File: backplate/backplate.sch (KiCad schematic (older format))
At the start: 1 part, among them J1 Conn_01x01_Male

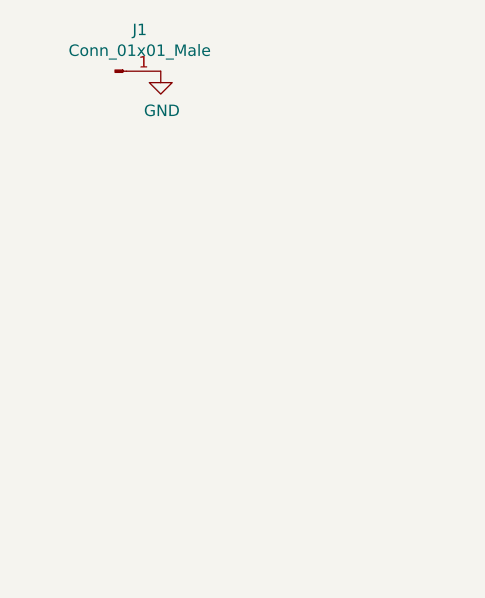
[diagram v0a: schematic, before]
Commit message: need to create models to check board compatibility; prototype candidate
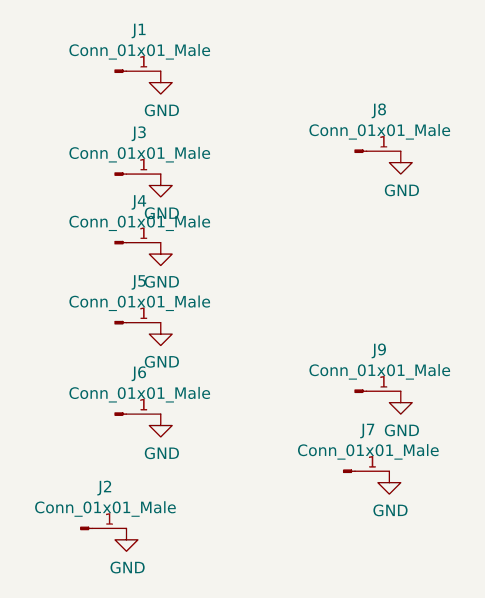
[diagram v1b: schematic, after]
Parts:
- added J2, J3, J4, J5, J6, J7, J8, J9: Conn_01x01_Male, backplate:sound_mounting_hole, symbol Connector:Conn_01x01_Male
- J1: footprint (none) -> backplate:sound_mounting_hole
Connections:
- net GND: now also J2.1 (Pin_1), J3.1 (Pin_1), J4.1 (Pin_1), J5.1 (Pin_1), J6.1 (Pin_1), J7.1 (Pin_1), J8.1 (Pin_1), J9.1 (Pin_1)
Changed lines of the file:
@@
 $EndDescr
-$Comp
-L Connector:Conn_01x01_Male J1
-U 1 1 5EB515EA
-P 3150 3350
-F 0 "J1" H 3258 3531 50  0000 C CNN
-F 1 "Conn_01x01_Male" H 3258 3440 50  0000 C CNN
-F 2 "" H 3150 3350 50  0001 C CNN
-F 3 "~" H 3150 3350 50  0001 C CNN
-	1    3150 3350
-	1    0    0    -1
-$EndComp
 $Comp
 L power:GND #PWR?
@@
 	1    0    0    -1
 $EndComp
+$Comp
+L Connector:Conn_01x01_Male J1
+U 1 1 5EB515EA
+P 3150 3350
+F 0 "J1" H 3258 3531 50  0000 C CNN
+F 1 "Conn_01x01_Male" H 3258 3440 50  0000 C CNN
+F 2 "backplate:sound_mounting_hole" H 3150 3350 50  0001 C CNN
+F 3 "~" H 3150 3350 50  0001 C CNN
+	1    3150 3350
+	1    0    0    -1
+$EndComp
+$Comp
+L power:GND #PWR?
+U 1 1 5EC17961
+P 3350 3800
+F 0 "#PWR?" H 3350 3550 50  0001 C CNN
+F 1 "GND" H 3355 3627 50  0000 C CNN
+F 2 "" H 3350 3800 50  0001 C CNN
+F 3 "" H 3350 3800 50  0001 C CNN
+	1    3350 3800
+	1    0    0    -1
+$EndComp
+$Comp
+L Connector:Conn_01x01_Male J3
+U 1 1 5EC17967
+P 3150 3800
+F 0 "J3" H 3258 3981 50  0000 C CNN
+F 1 "Conn_01x01_Male" H 3258 3890 50  0000 C CNN
+F 2 "backplate:sound_mounting_hole" H 3150 3800 50  0001 C CNN
+F 3 "~" H 3150 3800 50  0001 C CNN
+	1    3150 3800
+	1    0    0    -1
+$EndComp
+$Comp
+L power:GND #PWR?
+U 1 1 5EC17B1F
+P 3350 4100
+F 0 "#PWR?" H 3350 3850 50  0001 C CNN
+F 1 "GND" H 3355 3927 50  0000 C CNN
+F 2 "" H 3350 4100 50  0001 C CNN
+F 3 "" H 3350 4100 50  0001 C CNN
+	1    3350 4100
+	1    0    0    -1
+$EndComp
+$Comp
+L Connector:Conn_01x01_Male J4
+U 1 1 5EC17B25
+P 3150 4100
+F 0 "J4" H 3258 4281 50  0000 C CNN
+F 1 "Conn_01x01_Male" H 3258 4190 50  0000 C CNN
+F 2 "backplate:sound_mounting_hole" H 3150 4100 50  0001 C CNN
+F 3 "~" H 3150 4100 50  0001 C CNN
+	1    3150 4100
+	1    0    0    -1
+$EndComp
+$Comp
+L power:GND #PWR?
+U 1 1 5EC17CFB
+P 3350 4450
+F 0 "#PWR?" H 3350 4200 50  0001 C CNN
+F 1 "GND" H 3355 4277 50  0000 C CNN
+F 2 "" H 3350 4450 50  0001 C CNN
+F 3 "" H 3350 4450 50  0001 C CNN
+	1    3350 4450
+	1    0    0    -1
+$EndComp
+$Comp
+L Connector:Conn_01x01_Male J5
+U 1 1 5EC17D01
+P 3150 4450
+F 0 "J5" H 3258 4631 50  0000 C CNN
+F 1 "Conn_01x01_Male" H 3258 4540 50  0000 C CNN
+F 2 "backplate:sound_mounting_hole" H 3150 4450 50  0001 C CNN
+F 3 "~" H 3150 4450 50  0001 C CNN
+	1    3150 4450
+	1    0    0    -1
+$EndComp
+$Comp
+L power:GND #PWR?
+U 1 1 5EC1804B
+P 3350 4850
+F 0 "#PWR?" H 3350 4600 50  0001 C CNN
+F 1 "GND" H 3355 4677 50  0000 C CNN
+F 2 "" H 3350 4850 50  0001 C CNN
+F 3 "" H 3350 4850 50  0001 C CNN
+	1    3350 4850
+	1    0    0    -1
+$EndComp
+$Comp
+L Connector:Conn_01x01_Male J6
+U 1 1 5EC18051
+P 3150 4850
+F 0 "J6" H 3258 5031 50  0000 C CNN
+F 1 "Conn_01x01_Male" H 3258 4940 50  0000 C CNN
+F 2 "backplate:sound_mounting_hole" H 3150 4850 50  0001 C CNN
+F 3 "~" H 3150 4850 50  0001 C CNN
+	1    3150 4850
+	1    0    0    -1
+$EndComp
+$Comp
+L power:GND #PWR?
+U 1 1 5EC18207
+P 3200 5350
+F 0 "#PWR?" H 3200 5100 50  0001 C CNN
+F 1 "GND" H 3205 5177 50  0000 C CNN
+F 2 "" H 3200 5350 50  0001 C CNN
+F 3 "" H 3200 5350 50  0001 C CNN
+	1    3200 5350
+	1    0    0    -1
+$EndComp
+$Comp
+L Connector:Conn_01x01_Male J2
+U 1 1 5EC1820D
+P 3000 5350
+F 0 "J2" H 3108 5531 50  0000 C CNN
+F 1 "Conn_01x01_Male" H 3108 5440 50  0000 C CNN
+F 2 "backplate:sound_mounting_hole" H 3000 5350 50  0001 C CNN
+F 3 "~" H 3000 5350 50  0001 C CNN
+	1    3000 5350
+	1    0    0    -1
+$EndComp
+$Comp
+L power:GND #PWR?
+U 1 1 5EC182CD
+P 4400 4750
+F 0 "#PWR?" H 4400 4500 50  0001 C CNN
+F 1 "GND" H 4405 4577 50  0000 C CNN
+F 2 "" H 4400 4750 50  0001 C CNN
+F 3 "" H 4400 4750 50  0001 C CNN
+	1    4400 4750
+	1    0    0    -1
+$EndComp
+$Comp
+L Connector:Conn_01x01_Male J9
+U 1 1 5EC182D3
+P 4200 4750
+F 0 "J9" H 4308 4931 50  0000 C CNN
+F 1 "Conn_01x01_Male" H 4308 4840 50  0000 C CNN
+F 2 "backplate:sound_mounting_hole" H 4200 4750 50  0001 C CNN
+F 3 "~" H 4200 4750 50  0001 C CNN
+	1    4200 4750
+	1    0    0    -1
+$EndComp
+$Comp
+L power:GND #PWR?
+U 1 1 5EC183A7
+P 4400 3700
+F 0 "#PWR?" H 4400 3450 50  0001 C CNN
+F 1 "GND" H 4405 3527 50  0000 C CNN
+F 2 "" H 4400 3700 50  0001 C CNN
+F 3 "" H 4400 3700 50  0001 C CNN
+	1    4400 3700
+	1    0    0    -1
+$EndComp
+$Comp
+L Connector:Conn_01x01_Male J8
+U 1 1 5EC183AD
+P 4200 3700
+F 0 "J8" H 4308 3881 50  0000 C CNN
+F 1 "Conn_01x01_Male" H 4308 3790 50  0000 C CNN
+F 2 "backplate:sound_mounting_hole" H 4200 3700 50  0001 C CNN
+F 3 "~" H 4200 3700 50  0001 C CNN
+	1    4200 3700
+	1    0    0    -1
+$EndComp
+$Comp
+L power:GND #PWR?
+U 1 1 5EC184B9
+P 4350 5100
+F 0 "#PWR?" H 4350 4850 50  0001 C CNN
+F 1 "GND" H 4355 4927 50  0000 C CNN
+F 2 "" H 4350 5100 50  0001 C CNN
+F 3 "" H 4350 5100 50  0001 C CNN
+	1    4350 5100
+	1    0    0    -1
+$EndComp
+$Comp
+L Connector:Conn_01x01_Male J7
+U 1 1 5EC184BF
+P 4150 5100
+F 0 "J7" H 4258 5281 50  0000 C CNN
+F 1 "Conn_01x01_Male" H 4258 5190 50  0000 C CNN
+F 2 "backplate:sound_mounting_hole" H 4150 5100 50  0001 C CNN
+F 3 "~" H 4150 5100 50  0001 C CNN
+	1    4150 5100
+	1    0    0    -1
+$EndComp
